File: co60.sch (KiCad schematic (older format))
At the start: 12 parts, among them U1 ATMEGA32U4-AU, X1 ASX3F

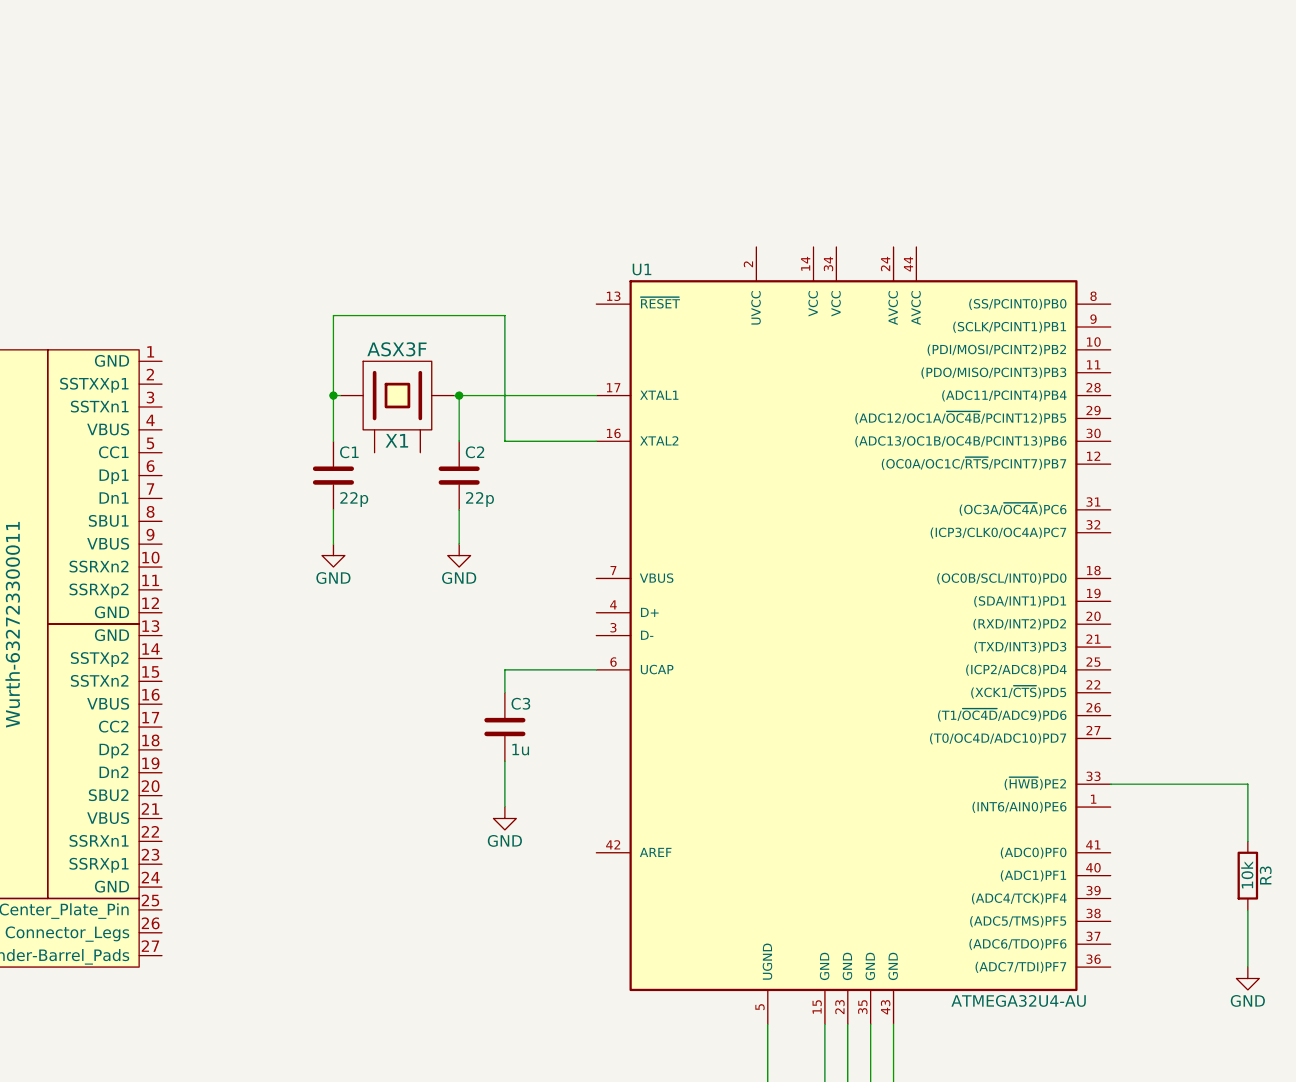
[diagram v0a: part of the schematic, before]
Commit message: Update: Work on switch matrix schematic
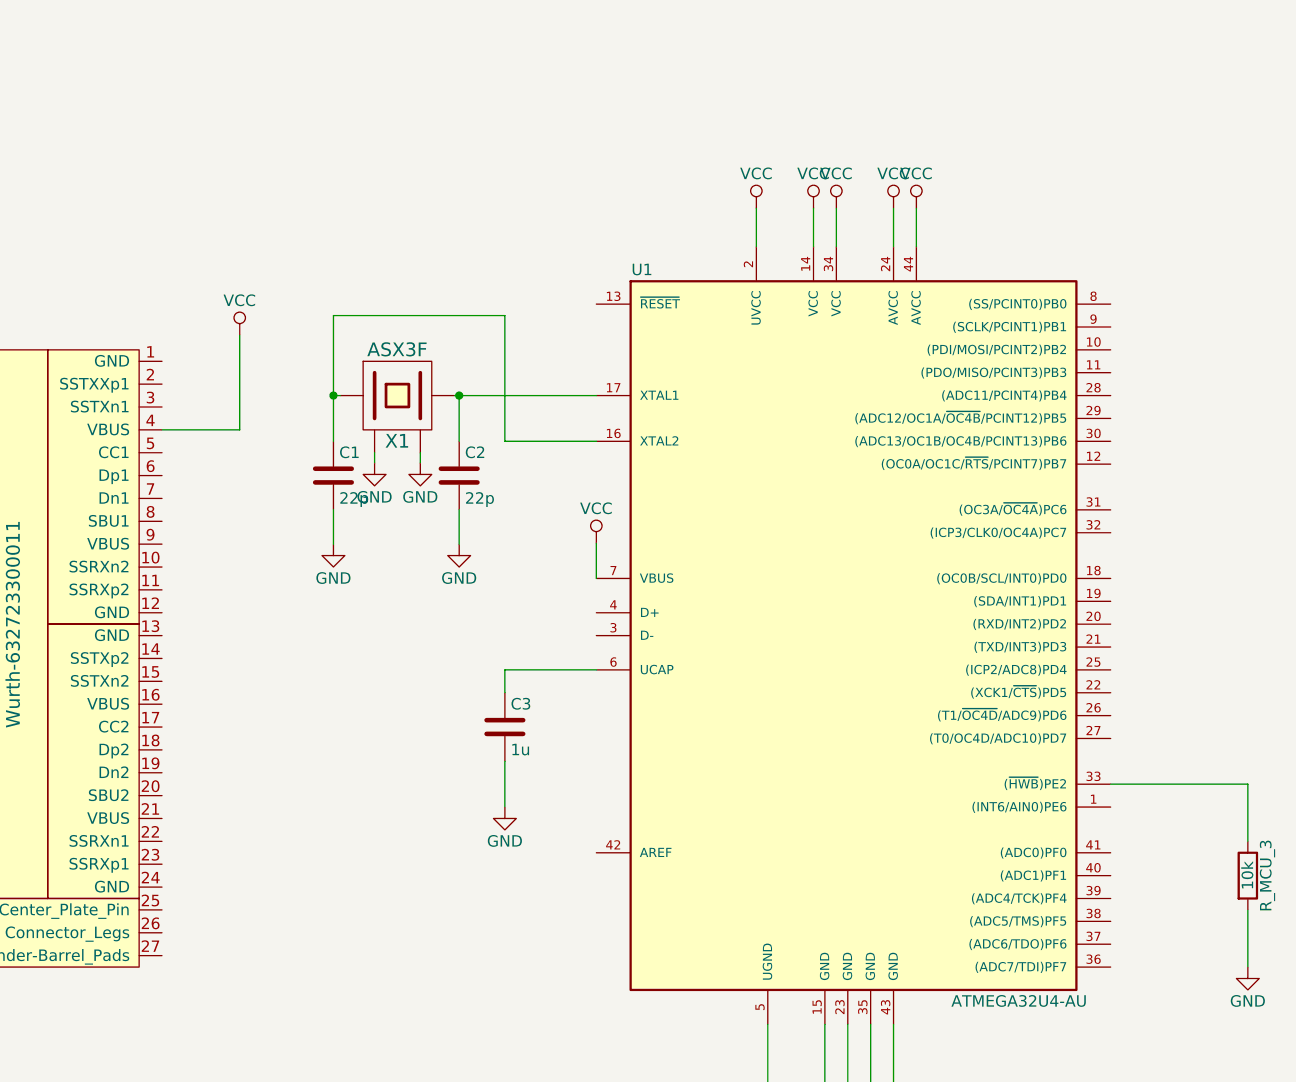
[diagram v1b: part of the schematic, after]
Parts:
- renumbered R3 to R_MCU_3
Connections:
- net GND: now also X1.2 (GND), X1.4 (GND)
- net VCC: now also U1.14 (VCC), U1.2 (UVCC), U1.24 (AVCC), U1.34 (VCC), U1.44 (AVCC), U1.7 (VBUS), USB1.4 (VBUS)
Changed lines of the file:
@@
 $EndComp
 $Comp
-L GND #PWR?
+L GND #PWR01
 U 1 1 5AAB4B68
 P 4150 3350
-F 0 "#PWR?" H 4150 3100 50  0001 C CNN
+F 0 "#PWR01" H 4150 3100 50  0001 C CNN
 F 1 "GND" H 4150 3200 50  0000 C CNN
 F 2 "" H 4150 3350 50  0001 C CNN
@@
 $EndComp
 $Comp
-L GND #PWR?
+L GND #PWR02
 U 1 1 5AAB4B9D
 P 3600 3350
-F 0 "#PWR?" H 3600 3100 50  0001 C CNN
+F 0 "#PWR02" H 3600 3100 50  0001 C CNN
 F 1 "GND" H 3600 3200 50  0000 C CNN
 F 2 "" H 3600 3350 50  0001 C CNN
@@
 $EndComp
 $Comp
-L GND #PWR?
+L GND #PWR03
 U 1 1 5AAB5020
 P 4350 4500
-F 0 "#PWR?" H 4350 4250 50  0001 C CNN
+F 0 "#PWR03" H 4350 4250 50  0001 C CNN
 F 1 "GND" H 4350 4350 50  0000 C CNN
 F 2 "" H 4350 4500 50  0001 C CNN
@@
 $EndComp
 $Comp
-L GND #PWR?
+L GND #PWR04
 U 1 1 5AAB51AD
 P 5500 5750
-F 0 "#PWR?" H 5500 5500 50  0001 C CNN
+F 0 "#PWR04" H 5500 5500 50  0001 C CNN
 F 1 "GND" H 5500 5600 50  0000 C CNN
 F 2 "" H 5500 5750 50  0001 C CNN
@@
 $EndComp
 $Comp
-L GND #PWR?
+L GND #PWR05
 U 1 1 5AAB51FB
 P 5750 5750
-F 0 "#PWR?" H 5750 5500 50  0001 C CNN
+F 0 "#PWR05" H 5750 5500 50  0001 C CNN
 F 1 "GND" H 5750 5600 50  0000 C CNN
 F 2 "" H 5750 5750 50  0001 C CNN
@@
 $EndComp
 $Comp
-L GND #PWR?
+L GND #PWR06
 U 1 1 5AAB5215
 P 5850 5750
-F 0 "#PWR?" H 5850 5500 50  0001 C CNN
+F 0 "#PWR06" H 5850 5500 50  0001 C CNN
 F 1 "GND" H 5850 5600 50  0000 C CNN
 F 2 "" H 5850 5750 50  0001 C CNN
@@
 $EndComp
 $Comp
-L GND #PWR?
+L GND #PWR07
 U 1 1 5AAB53E2
 P 5950 5750
-F 0 "#PWR?" H 5950 5500 50  0001 C CNN
+F 0 "#PWR07" H 5950 5500 50  0001 C CNN
 F 1 "GND" H 5950 5600 50  0000 C CNN
 F 2 "" H 5950 5750 50  0001 C CNN
@@
 $EndComp
 $Comp
-L GND #PWR?
+L GND #PWR08
 U 1 1 5AAB53FC
 P 6050 5750
-F 0 "#PWR?" H 6050 5500 50  0001 C CNN
+F 0 "#PWR08" H 6050 5500 50  0001 C CNN
 F 1 "GND" H 6050 5600 50  0000 C CNN
 F 2 "" H 6050 5750 50  0001 C CNN
@@
 $EndComp
 $Comp
-L GND #PWR?
+L GND #PWR09
 U 1 1 5AAB5D65
 P 900 1400
-F 0 "#PWR?" H 900 1150 50  0001 C CNN
+F 0 "#PWR09" H 900 1150 50  0001 C CNN
 F 1 "GND" H 900 1250 50  0000 C CNN
 F 2 "" H 900 1400 50  0001 C CNN
@@
 $EndComp
 $Comp
-L VCC #PWR?
+L VCC #PWR010
 U 1 1 5AAB5D97
 P 900 700
-F 0 "#PWR?" H 900 550 50  0001 C CNN
+F 0 "#PWR010" H 900 550 50  0001 C CNN
 F 1 "VCC" H 900 850 50  0000 C CNN
 F 2 "" H 900 700 50  0001 C CNN
@@
 $EndSheet
 $Comp
-L R R3
+L R R_MCU_3
 U 1 1 5AAF0E91
 P 7600 4800
-F 0 "R3" V 7680 4800 50  0000 C CNN
+F 0 "R_MCU_3" V 7680 4800 50  0000 C CNN
 F 1 "10k" V 7600 4800 50  0000 C CNN
 F 2 "" V 7530 4800 50  0001 C CNN
@@
 $EndComp
 $Comp
-L GND #PWR?
+L GND #PWR011
 U 1 1 5AAF11DE
 P 7600 5200
-F 0 "#PWR?" H 7600 4950 50  0001 C CNN
+F 0 "#PWR011" H 7600 4950 50  0001 C CNN
 F 1 "GND" H 7600 5050 50  0000 C CNN
 F 2 "" H 7600 5200 50  0001 C CNN
@@
 	3630 2700 3600 2700
 Connection ~ 3600 2700
+$Comp
+L VCC #PWR012
+U 1 1 5B32978F
+P 6150 1880
+F 0 "#PWR012" H 6150 1730 50  0001 C CNN
+F 1 "VCC" H 6150 2030 50  0000 C CNN
+F 2 "" H 6150 1880 50  0001 C CNN
+F 3 "" H 6150 1880 50  0001 C CNN
+	1    6150 1880
+	1    0    0    -1
+$EndComp
+$Comp
+L VCC #PWR013
+U 1 1 5B3297C5
+P 6050 1880
+F 0 "#PWR013" H 6050 1730 50  0001 C CNN
+F 1 "VCC" H 6050 2030 50  0000 C CNN
+F 2 "" H 6050 1880 50  0001 C CNN
+F 3 "" H 6050 1880 50  0001 C CNN
+	1    6050 1880
+	1    0    0    -1
+$EndComp
+$Comp
+L VCC #PWR014
+U 1 1 5B3297F4
+P 5800 1880
+F 0 "#PWR014" H 5800 1730 50  0001 C CNN
+F 1 "VCC" H 5800 2030 50  0000 C CNN
+F 2 "" H 5800 1880 50  0001 C CNN
+F 3 "" H 5800 1880 50  0001 C CNN
+	1    5800 1880
+	1    0    0    -1
+$EndComp
+$Comp
+L VCC #PWR015
+U 1 1 5B329823
+P 5700 1880
+F 0 "#PWR015" H 5700 1730 50  0001 C CNN
+F 1 "VCC" H 5700 2030 50  0000 C CNN
+F 2 "" H 5700 1880 50  0001 C CNN
+F 3 "" H 5700 1880 50  0001 C CNN
+	1    5700 1880
+	1    0    0    -1
+$EndComp
+$Comp
+L VCC #PWR016
+U 1 1 5B329CEA
+P 5450 1880
+F 0 "#PWR016" H 5450 1730 50  0001 C CNN
+F 1 "VCC" H 5450 2030 50  0000 C CNN
+F 2 "" H 5450 1880 50  0001 C CNN
+F 3 "" H 5450 1880 50  0001 C CNN
+	1    5450 1880
+	1    0    0    -1
+$EndComp
+Wire Wire Line
+	5450 1880 5450 2050
+Wire Wire Line
+	5700 1880 5700 2050
+Wire Wire Line
+	5800 1880 5800 2050
+Wire Wire Line
+	6050 1880 6050 2050
+Wire Wire Line
+	6150 1880 6150 2050
+$Comp
+L VCC #PWR017
+U 1 1 5B32C5A6
+P 4750 3345
+F 0 "#PWR017" H 4750 3195 50  0001 C CNN
+F 1 "VCC" H 4750 3495 50  0000 C CNN
+F 2 "" H 4750 3345 50  0001 C CNN
+F 3 "" H 4750 3345 50  0001 C CNN
+	1    4750 3345
+	1    0    0    -1
+$EndComp
+Wire Wire Line
+	4750 3345 4750 3500
+$Comp
+L VCC #PWR018
+U 1 1 5B368741
+P 3190 2435
+F 0 "#PWR018" H 3190 2285 50  0001 C CNN
+F 1 "VCC" H 3190 2585 50  0000 C CNN
+F 2 "" H 3190 2435 50  0001 C CNN
+F 3 "" H 3190 2435 50  0001 C CNN
+	1    3190 2435
+	1    0    0    -1
+$EndComp
+Wire Wire Line
+	2850 2850 3190 2850
+Wire Wire Line
+	3190 2850 3190 2435
+$Comp
+L GND #PWR?
+U 1 1 5B375157
+P 3780 2995
+F 0 "#PWR?" H 3780 2745 50  0001 C CNN
+F 1 "GND" H 3780 2845 50  0000 C CNN
+F 2 "" H 3780 2995 50  0001 C CNN
+F 3 "" H 3780 2995 50  0001 C CNN
+	1    3780 2995
+	1    0    0    -1
+$EndComp
+$Comp
+L GND #PWR?
+U 1 1 5B375186
+P 3980 2995
+F 0 "#PWR?" H 3980 2745 50  0001 C CNN
+F 1 "GND" H 3980 2845 50  0000 C CNN
+F 2 "" H 3980 2995 50  0001 C CNN
+F 3 "" H 3980 2995 50  0001 C CNN
+	1    3980 2995
+	1    0    0    -1
+$EndComp
+Wire Wire Line
+	3780 2950 3780 2995
+Wire Wire Line
+	3980 2950 3980 2995
 $EndSCHEMATC

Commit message: Update: More work on schematic connections. Not finished yet
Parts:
- added R_MCU_4: 10k, symbol R
- added R_USB_1, R_USB_2: 22, symbol R
- added R_USB_3, R_USB_4: 5.1k, symbol R
- added SW1: SW_Push, symbol SW_Push
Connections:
- net GND: now also USB1.1 (GND), USB1.12 (GND), USB1.13 (GND), USB1.24 (GND), R_USB_3.2, R_USB_4.2, SW1.1
- net VCC: now also USB1.16 (VBUS), USB1.21 (VBUS), USB1.9 (VBUS), R_MCU_4.1
- net COL2: now reaches U1.1 ((INT6/AIN0)PE6)
- net COL8: now reaches U1.10 ((PDI/MOSI/PCINT2)PB2)
- net COL13: now reaches U1.11 ((PDO/MISO/PCINT3)PB3)
- net LEDPWM: now reaches U1.12 ((OC0A/OC1C/~RTS~/PCINT7)PB7)
- net at U1.13 (~RESET~): now also R_MCU_4.2, SW1.2
- net ROW0: now reaches U1.18 ((OC0B/SCL/INT0)PD0)
- net ROW1: now reaches U1.19 ((SDA/INT1)PD1)
- net ROW2: now reaches U1.20 ((RXD/INT2)PD2)
- net ROW3: now reaches U1.21 ((TXD/INT3)PD3)
- net ROW4: now reaches U1.22 ((XCK1/~CTS~)PD5)
- net COL6: now reaches U1.25 ((ICP2/ADC8)PD4)
- net COL12: now reaches U1.26 ((T1/~OC4D~/ADC9)PD6)
- net COL11: now reaches U1.27 ((T0/OC4D/ADC10)PD7)
- net COL10: now reaches U1.28 ((ADC11/PCINT4)PB4)
- net COL9: now reaches U1.29 ((ADC12/OC1A/~OC4B~/PCINT12)PB5)
- net at U1.3 (D-): now also R_USB_2.1
- net COL5: now reaches U1.30 ((ADC13/OC1B/OC4B/PCINT13)PB6)
- net COL4: now reaches U1.31 ((OC3A/~OC4A~)PC6)
- net COL3: now reaches U1.32 ((ICP3/CLK0/OC4A)PC7)
- net at U1.4 (D+): now also R_USB_1.1
- net COL1: now reaches U1.40 ((ADC1)PF1)
- net COL0: now reaches U1.41 ((ADC0)PF0)
- net COL14: now reaches U1.8 ((SS/PCINT0)PB0)
- net COL7: now reaches U1.9 ((SCLK/PCINT1)PB1)
- net at USB1.17 (CC2): now also R_USB_4.1
- net at USB1.18 (Dp2): now also USB1.6 (Dp1), R_USB_1.2
- net at USB1.19 (Dn2): now also USB1.7 (Dn1), R_USB_2.2
- net at USB1.5 (CC1): now also R_USB_3.1
- no-connect marks 0 -> 15
